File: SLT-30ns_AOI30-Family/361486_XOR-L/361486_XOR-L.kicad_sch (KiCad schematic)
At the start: 8 parts, among them T1 IBM_Transistor, T2 IBM_Transistor, T3 IBM_Transistor, U1 12-Pin_SLx_Can

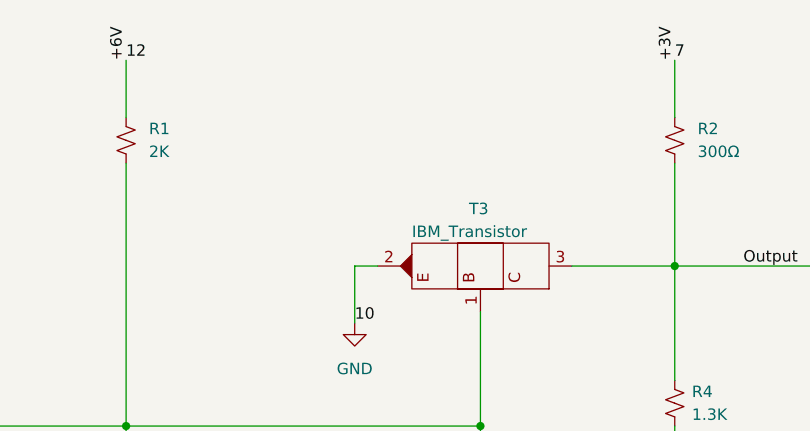
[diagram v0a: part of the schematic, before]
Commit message: Update schematic pdfs
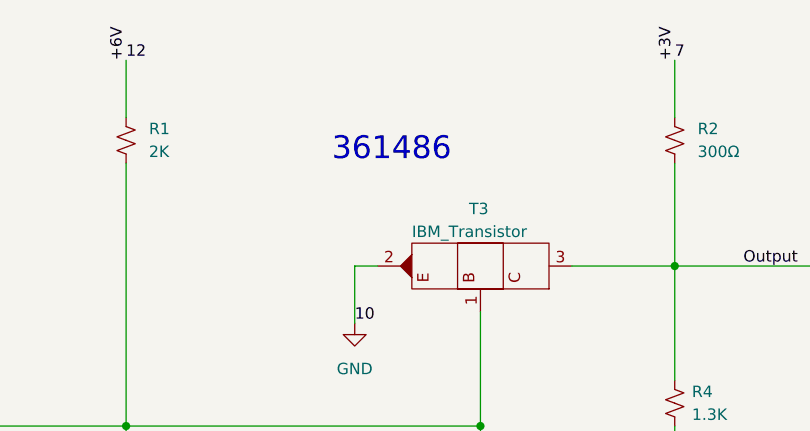
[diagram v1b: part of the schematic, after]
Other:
- note added: "361486"
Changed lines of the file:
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@@
     (stroke (width 0) (type default) (color 0 0 0 0))
+  )
+  (text "361486" (at 107.95 74.93 0)
+    (effects (font (size 2.54 2.54)) (justify left bottom))
   )
   (label "8" (at 166.37 86.36 0)
